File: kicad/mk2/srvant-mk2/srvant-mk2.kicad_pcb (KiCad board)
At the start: 2 copper layers, 5.9 x 5.8 mm, 245 parts, among them J1 Barrel_Jack_Switch, J10 HDMI connector, J2 Conn_01x02, J3 Conn_01x03, J4 USB_OTG, J5 ARJM11, J6 Conn_02x05_Odd_Even, J7 USB[690-008-221-904], J8 Bus_M.2_Socket_M, J9 ARJM11, Q1 DMP3013SFV-7, SW1 SW_DIP_x04, U1 AP63205WU, U10 TPD4EUSB30, U11 TPD4EUSB30, U12 KSZ9131RNXI-TR, U13 RT9742SNGV, U14 AP22653W6, U15 TLV62585DRLR, U16 FSUSB42MUX, U17 USB2514B-I/M2, U18 74LVC1G07SE-7, U19 TPD4EUSB30, U2 AP64501SP-13, U20 TPD4EUSB30, U3 74AHC1G32, U4 INA219AxDCN, U5 rp-t113-s3, U6 PCF85063AT/AAZ, U7 TPD4EUSB30, U8 74LVC2G07, U9 AP22653W6, Y1 X32K768S301, Y2 25Mhz, Y3 24MHz

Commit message: save state
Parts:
- removed C42, C92, C93: 100n, Capacitor_SMD:C_0402_1005Metric
- removed C83, C84, C85, C86, C87, C91: 10u, Capacitor_SMD:C_0805_2012Metric
- removed FB4, FB6, FB7: 220R, Resistor_SMD:R_0402_1005Metric
- removed J6: Conn_02x05_Odd_Even, Connector_PinHeader_2.54mm:PinHeader_2x05_P2.54mm_Vertical
- removed J7: USB[690-008-221-904], footprints:MOLEX_USB_67298-4090
- removed R26, R31, R35, R43, R45, R52: 10K, Resistor_SMD:R_0402_1005Metric
- removed R27, R32, R49: 1K, Resistor_SMD:R_0402_1005Metric
- removed R56: 22K 1%, Resistor_SMD:R_0402_1005Metric
- removed R61: 36K/1%, Resistor_SMD:R_0402_1005Metric
- removed TP13: TestPoint, TestPoint:TestPoint_Pad_2.0x2.0mm
- removed TP7, TP8, TP9: TestPoint, TestPoint:TestPoint_Pad_D1.0mm
- added D9: PESD2USB5UX-T, Package_TO_SOT_SMD:SOT-23, F.Cu at (84.8, 54.9)
- added FB9: 220R, Resistor_SMD:R_0402_1005Metric, F.Cu at (35.4, 177.3)
- added J11: USB A, footprints:CONN_GSB19110KEU_AMP, F.Cu at (39.4, 186.6)
- added R57: 510K 1%, Resistor_SMD:R_0402_1005Metric, F.Cu at (30.2, 60.2)
- added R69: 0, Resistor_SMD:R_0402_1005Metric, F.Cu at (44.1, 123.5)
- added R70: 0, Resistor_SMD:R_0402_1005Metric, F.Cu at (43.0, 123.5)
- added R71: 3.3K, Resistor_SMD:R_0402_1005Metric, F.Cu at (27.1, 136.6)
- added R72: 3.3K, Resistor_SMD:R_0402_1005Metric, F.Cu at (27.1, 138.1)
- added R73: 0, Resistor_SMD:R_0402_1005Metric, F.Cu at (81.9, 56.9)
- added SW2: EMMC_KEY, button-1571563-4:SW4_FSM-5P23_TEC, F.Cu at (82.4, 45.8)
- added SW3: RST, button-1571563-4:SW4_FSM-5P23_TEC, F.Cu at (89.9, 45.9)
- added SW4: HOST_RESET, footprints:button-SW_TL3340AF160QG, F.Cu at (46.9, 196.3)
- added TP16: +5v BMC, TestPoint:TestPoint_Pad_D1.0mm, B.Cu at (25.6, 78.4)
- added TP17: 5v OTG, TestPoint:TestPoint_Pad_D1.0mm, B.Cu at (52.9, 40.4)
- added TP18: ~, TestPoint:TestPoint_Pad_1.0x1.0mm, B.Cu at (45.8, 167.5)
- added TP19: NMI_N, TestPoint:TestPoint_Pad_D1.0mm, B.Cu at (33.2, 42.5)
- added U21: 74LVC1G07SE-7, Package_TO_SOT_SMD:SOT-353_SC-70-5, F.Cu at (27.1, 58.1)
- added U22: TMP1075DSG, Package_SON:WSON-8-1EP_2x2mm_P0.5mm_EP0.9x1.6mm_ThermalVias, F.Cu at (33.8, 123.6)
- added U23: SLB9670VQ20FW785XTMA1, QFN32_SLB9670VQ20FW785XTMA1_INF:QFN32_SLB9670VQ20FW785XTMA1_INF, F.Cu at (20.0, 109.5)
- added U24: 74AHC1G08, Package_TO_SOT_SMD:SOT-23-5_HandSoldering, F.Cu at (34.0, 58.2)
- added U25: 74AHC1G08, Package_TO_SOT_SMD:SOT-23-5, F.Cu at (79.2, 56.4)
- C33: value 10u -> 10u/35v; footprint Capacitor_SMD:C_0805_2012Metric -> Capacitor_SMD:C_0402_1005Metric
- C34: value 100u -> 100n; footprint Capacitor_Tantalum_SMD:CP_EIA-7343-31_Kemet-D -> Capacitor_SMD:C_0402_1005Metric
- C35, C36, C38, C39, C82, C90: value 10u -> 100n; footprint Capacitor_SMD:C_0805_2012Metric -> Capacitor_SMD:C_0402_1005Metric
- C40, C58, C59, C60, C61, C62: value 10u/35v -> 100n
- C49, C52, C53, C54, C56: value 100n -> 10u/35v
- C67, C68: value 100n -> 15p
- C69, C71: value 100n -> 10u 35v; footprint Capacitor_SMD:C_0402_1005Metric -> Capacitor_SMD:C_0805_2012Metric
- C70, C78, C79: value 100n -> 10u; footprint Capacitor_SMD:C_0402_1005Metric -> Capacitor_SMD:C_0805_2012Metric
- C73: value 15p -> 100n
- C74: value 15p -> 100u; footprint Capacitor_SMD:C_0402_1005Metric -> Capacitor_Tantalum_SMD:CP_EIA-7343-31_Kemet-D
- C75, C77: value 10u 35v -> 10u
- C80: value 100u -> 10u; footprint Capacitor_Tantalum_SMD:CP_EIA-7343-31_Kemet-D -> Capacitor_SMD:C_0805_2012Metric
- C88, C89: value 27p -> 100n
- C94: value 100n -> 1u; footprint Capacitor_SMD:C_0402_1005Metric -> Capacitor_SMD:C_0805_2012Metric
- R15: value 15K/1% -> 330R
- R18: value 330R -> 22R
- R24, R42: value 22R -> 10K
- R28, R33, R47, R50: value 10K -> 1K
- R29: value 1K -> 6.04K
- R30: value 6.04K -> 10K
- R34, R44, R46, R51: value 1K -> 10K
- R36: value 1K -> 22R
- R53: value 1K -> 15K/1%
- R54: value 15K/1% -> 100K 1%
- R55: value 100K 1% -> 22K 1%
- R59: value 36K/1% -> 510K 1%
- R62, R64: value 36K/1% -> 0
- R63: value 12K/1% -> 0
- SW1: value SW_DIP_x04 -> POWER; footprint DIP_SWITCH_DS04-254-2-04BK-SMT:DS04-254-2-04BK-SMT_CUD -> footprints:button-SW_TL3340AF160QG
- TP1: value TestPoint (VIN) -> VIN; moved to B.Cu
- TP10: value TestPoint -> PHY_AVDDH(3.3v); moved to B.Cu
- TP11: footprint TestPoint:TestPoint_Pad_2.0x2.0mm -> TestPoint:TestPoint_Pad_D1.0mm; moved to B.Cu
- TP12: value TestPoint -> 3v3_PCIe; footprint TestPoint:TestPoint_Pad_1.5x1.5mm -> TestPoint:TestPoint_Pad_D1.0mm; moved to B.Cu
- TP14: value TestPoint -> PCIe_nCLKREQ; footprint TestPoint:TestPoint_Pad_2.0x2.0mm -> TestPoint:TestPoint_Pad_D1.0mm; moved to B.Cu
- TP15: value TestPoint -> PCIe_nRST; footprint TestPoint:TestPoint_Pad_2.0x2.0mm -> TestPoint:TestPoint_Pad_D1.0mm; moved to B.Cu
- TP2: value TestPoint -> +5v HOST; moved to B.Cu
- TP3: value TestPoint -> GND; footprint TestPoint:TestPoint_Pad_2.0x2.0mm -> TestPoint:TestPoint_Pad_D1.0mm; moved to B.Cu
- TP4: value TestPoint -> 1v2; footprint TestPoint:TestPoint_Pad_2.0x2.0mm -> TestPoint:TestPoint_Pad_D1.0mm; moved to B.Cu
- TP5: value TestPoint -> 3.3v BMC; footprint TestPoint:TestPoint_Pad_2.0x2.0mm -> TestPoint:TestPoint_Pad_D1.0mm; moved to B.Cu
- TP6: value TestPoint -> VIN; moved to B.Cu
- U13: value RT9742SNGV -> 74AHC1G04; footprint Package_TO_SOT_SMD:SOT-23 -> Package_TO_SOT_SMD:SOT-23-5
- U17: value USB2514B-I/M2 -> PCF85063AT/AAZ; footprint Package_DFN_QFN:QFN-36-1EP_6x6mm_P0.5mm_EP3.7x3.7mm -> Package_SO:SOIC-8_3.9x4.9mm_P1.27mm
- U9: value AP22653W6 -> RT9742SNGV; footprint Package_TO_SOT_SMD:SOT-23-6 -> Package_TO_SOT_SMD:SOT-23
- Y3: value 24MHz -> X32K768S301; footprint footprints:LFXTAL-25MHz -> Crystal:Crystal_SMD_3215-2Pin_3.2x1.5mm
- moved C37 203.1 mm to (14.7, 147.5)
- moved R9 201.1 mm to (27.1, 145.8)
- moved R10 200.5 mm to (27.1, 146.9)
- moved D6 196.9 mm to (69.3, 183.5), turned to 90 degrees
- moved TP4 192.6 mm to (68.5, 180.6), turned to 180 degrees
- moved R13 191.3 mm to (16.7, 149.1)
- moved R14 191.0 mm to (16.7, 150.7)
- moved U13 189.8 mm to (41.8, 169.3), turned to 180 degrees
- moved C33 184.5 mm to (60.4, 164.6), turned to 180 degrees
- moved R6 184.3 mm to (13.1, 77.9), turned to 90 degrees
- moved U8 184.1 mm to (14.1, 144.9), turned to -90 degrees
- moved C34 183.8 mm to (60.4, 165.7), turned to 180 degrees
- moved D3 183.6 mm to (14.0, 149.1), turned to 180 degrees
- moved R11 182.1 mm to (27.1, 143.0), turned to 180 degrees
- moved C36 180.1 mm to (62.7, 164.6), turned to 180 degrees
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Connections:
- net /bmc/EPHY_25M renamed /BMC ethernet/EPHY_25M
- net /bmc/RESET_OUT_N renamed /BMC ethernet/RESET_OUT_N
- net /bmc/TXRXA_N renamed /BMC ethernet/TXRXA_N
- net /bmc/TXRXA_P renamed /BMC ethernet/TXRXA_P
- net /bmc/TXRXB_N renamed /BMC ethernet/TXRXB_N
- net /bmc/TXRXB_P renamed /BMC ethernet/TXRXB_P
- net /bmc/TXRXC_N renamed /BMC ethernet/TXRXC_N
- net /bmc/TXRXC_P renamed /BMC ethernet/TXRXC_P
- net /bmc/TXRXD_N renamed /BMC ethernet/TXRXD_N
- net /bmc/TXRXD_P renamed /BMC ethernet/TXRXD_P
- net /cm4/GPIO12 renamed /cm4/HOST_SDA5
- net /cm4/GPIO13 renamed /cm4/HOST_SCL5
- net /cm4/GPIO4 renamed /cm4/HOST_SPI4_CE0
- net /cm4/GPIO5 renamed /cm4/HOST_SPI4_MISO
- net /cm4/GPIO6 renamed /cm4/HOST_SPI4_MOSI
- net /cm4/GPIO7 renamed /cm4/HOST_SPI4_SCLK
- C100 pad 1: /cm4/+3V3 PCIe -> /cm4/+3.3v_HOST_PCIe
- C101 pad 1: /cm4/+3V3 PCIe -> /cm4/+3.3v_HOST_PCIe
- C102 pad 1: /cm4/+3V3 PCIe -> /cm4/+3.3v_HOST_PCIe
- C103 pad 1: /cm4/+3V3 PCIe -> /cm4/+3.3v_HOST_PCIe
- C20 pad 1: /power/+5v_HOST -> /cm4/+5v_HOST
- C23 pad 1: /power/+5v_HOST -> /cm4/+5v_HOST
- C25 pad 1: /power/+5v_HOST -> /cm4/+5v_HOST
- C26 pad 1: /power/+5v_HOST -> /cm4/+5v_HOST
- C27 pad 1: /power/+5v_HOST -> /cm4/+5v_HOST
- C28 pad 1: /power/+5v_HOST -> /cm4/+5v_HOST
- C30 pad 1: /bmc/3.3v_BMC -> /BMC ethernet/3.3v_BMC
- C31 pad 1: /bmc/3.3v_BMC -> /BMC ethernet/3.3v_BMC
- C33 pad 1: /bmc/+5v_BMC -> /BMC ethernet/1V2
- C34 pad 1: /bmc/+5V_OTG -> /BMC ethernet/1V2
- C35 pad 1: /bmc/+5V_OTG -> /BMC ethernet/1V2
- C36 pad 1: /bmc/+5V_OTG -> /BMC ethernet/1V2
- C37 pad 1: /bmc/3.3v_BMC -> /BMC ethernet/3.3v_BMC
- C38 pad 1: /bmc/+5V_OTG -> /BMC ethernet/1V2
- C39 pad 1: /bmc/+5V_OTG -> /BMC ethernet/1V2
- C40 pad 1: /bmc/PHY_DVDDL -> Net-(C40-Pad1)
- C41 pad 1: /bmc/PHY_DVDDL -> /BMC ethernet/1V2
- C43 pad 1: /bmc/PHY_DVDDL -> /BMC ethernet/1V2
- C44 pad 1: /bmc/PHY_AVDDL_PLL -> Net-(C44-Pad1)
- C45 pad 1: /bmc/PHY_DVDDL -> /BMC ethernet/1V2
- C46 pad 1: Net-(C46-Pad1) -> /BMC ethernet/1V2
- C47 pad 1: /bmc/PHY_AVDDL -> /BMC ethernet/1V2
- C48 pad 1: /bmc/PHY_AVDDL_PLL -> /BMC ethernet/1V2
- C49 pad 1: /bmc/PHY_DVDDL -> /BMC ethernet/1V2
- C50 pad 1: Net-(C50-Pad1) -> /BMC ethernet/1V2
- C51 pad 1: /bmc/PHY_AVDDL -> /BMC ethernet/1V2
- C52 pad 1: /bmc/PHY_AVDDL_PLL -> /BMC ethernet/1V2
- C53 pad 1: /bmc/PHY_DVDDL -> /BMC ethernet/PHY_RESET_N
- C54 pad 1: /bmc/PHY_AVDDL -> /BMC ethernet/3.3v_PHY
- C55 pad 1: /bmc/PHY_AVDDL_PLL -> Net-(U12-LDO_O)
- C56 pad 1: /bmc/PHY_DVDDL -> /BMC ethernet/3.3v_PHY
- C57 pad 1: /bmc/PHY_AVDDL -> /BMC ethernet/3.3v_PHY
- C58 pad 1: /bmc/PHY_AVDDL -> Net-(U12-LDO_O)
- C59 pad 1: /bmc/PHY_RESET_N -> /BMC ethernet/3.3v_PHY
- C60 pad 1: /bmc/PHY_AVDDH -> /BMC ethernet/3.3v_PHY
- C61 pad 1: /bmc/1V2 -> /BMC ethernet/3.3v_PHY
- C62 pad 1: /bmc/PHY_DVDDH -> /BMC ethernet/3.3v_PHY
- C63 pad 1: /bmc/PHY_AVDDH -> /BMC ethernet/3.3v_PHY
- C64 pad 1: /bmc/1V2 -> /BMC ethernet/3.3v_PHY
- C65 pad 1: /bmc/PHY_DVDDH -> /BMC ethernet/3.3v_PHY
- C66 pad 1: /bmc/PHY_AVDDH -> /BMC ethernet/3.3v_PHY
- C67 pad 1: /bmc/PHY_DVDDH -> GND
- C67 pad 2: GND -> Net-(U12-XI)
- C68 pad 1: /bmc/PHY_AVDDH -> Net-(U12-XO)
- C69 pad 1: /bmc/PHY_DVDDH -> /cm4/+5v_HOST
- C70 pad 1: /bmc/PHY_AVDDH -> /cm4/+5v_HOST
- C71 pad 1: /bmc/PHY_DVDDH -> /cm4/+5v_HOST
- C72 pad 1: /bmc/PHY_DVDDH -> /cm4/+5v_HOST
- C73 pad 1: GND -> /cm4/+5v_HOST_HDMI
- C73 pad 2: Net-(U12-XI) -> GND
- C74 pad 1: Net-(U12-XO) -> /cm4/+5v_HOST_VBUS
- C75 pad 1: /cm4/+5v_HOST -> /cm4/+5v_HOST_VBUS
- C76 pad 1: /cm4/+5v_HOST -> /cm4/+3.3v_HOST_PCIe
- C77 pad 1: /cm4/+5v_HOST -> /cm4/+5v_HOST_VBUS
- C78 pad 1: /cm4/+5v_HOST -> /cm4/+3.3v_HOST_PCIe
- C79 pad 1: /cm4/HDMI_5v -> /cm4/+5v_HOST_VBUS
- C80 pad 1: /cm4/VBUS -> /cm4/+3.3v_HOST_PCIe
- C81 pad 1: /cm4/VBUS -> /cm4/+5v_HOST_VBUS
- C82 pad 1: /cm4/VBUS -> /BMC ethernet/3.3v_BMC
- C88 pad 1: /cm4/XTALIN -> /cm4/+BATT
- C89 pad 1: /cm4/XTALOUT -> /cm4/+5v_HOST
- C90 pad 1: /cm4/+3.3v_HOST -> Net-(C90-Pad1)
- C90 pad 2: GND -> Net-(C90-Pad2)
- C95 pad 1: /cm4/+3.3v_HOST -> GND
- C95 pad 2: GND -> /cm4/+3.3v_HOST
- C96 pad 1: /cm4/+3.3v_HOST -> GND
- C96 pad 2: GND -> /cm4/+3.3v_HOST
- C97 pad 1: /cm4/+3.3v_HOST -> GND
- C97 pad 2: GND -> /cm4/+3.3v_HOST
- C98 pad 1: /cm4/+3V3 PCIe -> /cm4/+3.3v_HOST_PCIe
- C99 pad 1: /cm4/+3V3 PCIe -> /cm4/+3.3v_HOST_PCIe
- D2 pad 2: /bmc/3.3v_BMC -> /BMC ethernet/3.3v_BMC
- D3 pad 2: /bmc/3.3v_BMC -> /BMC ethernet/3.3v_BMC
- D4 pad 2: /bmc/+3.3v -> /BMC ethernet/3.3v_BMC
- D5 pad 1: /bmc/PHY_DVDDH -> /BMC ethernet/3.3v_PHY
- D5 pad 2: /bmc/PHY_RESET_N -> /BMC ethernet/PHY_RESET_N
- D6 pad 2: /bmc/PHY_RESET_N -> /BMC ethernet/PHY_RESET_N
- FB2 pad 1: /bmc/1V2 -> /BMC ethernet/3.3v_PHY
- FB2 pad 2: /bmc/PHY_DVDDL -> /BMC ethernet/3.3v_BMC
- FB3 pad 1: /bmc/1V2 -> Net-(U12-LDO_O)
- FB3 pad 2: /bmc/PHY_AVDDL_PLL -> /BMC ethernet/1V2
- J10 pad 18: /cm4/HDMI_5v -> /cm4/+5v_HOST_HDMI
- J2 pad 2: /bmc/3.3v_BMC -> /BMC ethernet/3.3v_BMC
- J4 pad 1: /bmc/+5V_OTG -> /bmc/+5V_BMC_OTG
- J5 pad 11: /bmc/PHY_DVDDH -> /BMC ethernet/3.3v_PHY
- J5 pad 13: /bmc/PHY_DVDDH -> /BMC ethernet/3.3v_PHY
- J5 pad 5: Net-(C46-Pad1) -> Net-(C40-Pad1)
- J5 pad 6: Net-(C50-Pad1) -> Net-(C44-Pad1)
- J8 pad 12: /cm4/+3V3 PCIe -> /cm4/+3.3v_HOST_PCIe
- J8 pad 14: /cm4/+3V3 PCIe -> /cm4/+3.3v_HOST_PCIe
- J8 pad 16: /cm4/+3V3 PCIe -> /cm4/+3.3v_HOST_PCIe
- J8 pad 18: /cm4/+3V3 PCIe -> /cm4/+3.3v_HOST_PCIe
- J8 pad 2: /cm4/+3V3 PCIe -> /cm4/+3.3v_HOST_PCIe
- J8 pad 4: /cm4/+3V3 PCIe -> /cm4/+3.3v_HOST_PCIe
- J8 pad 70: /cm4/+3V3 PCIe -> /cm4/+3.3v_HOST_PCIe
- J8 pad 72: /cm4/+3V3 PCIe -> /cm4/+3.3v_HOST_PCIe
- J8 pad 74: /cm4/+3V3 PCIe -> /cm4/+3.3v_HOST_PCIe
- L2 pad 2: /power/+5v_HOST -> /cm4/+5v_HOST
- L3 pad 2: /cm4/+3V3 PCIe -> /cm4/+3.3v_HOST_PCIe
- Module1 pad 20: /cm4/EEPROM_nWP -> /bmc/BMC_HOST_EEPROM_nWP
- Module1 pad 25: /cm4/GPIO21 -> /cm4/HOST_SPI1_SCLK
- Module1 pad 26: /cm4/GPIO19 -> /cm4/HOST_SPI1_MISO
- Module1 pad 27: /cm4/GPIO20 -> /cm4/HOST_SPI1_MOSI
- Module1 pad 39: /cm4/GPIO8 -> /bmc/BMC_UART1_RX
- Module1 pad 40: /cm4/GPIO9 -> /bmc/BMC_UART1_TX
- Module1 pad 49: /cm4/GPIO18 -> /cm4/HOST_SPI1_CE0_N
- Module1 pad 51: /cm4/HOST_UART_TX -> /bmc/BMC_UART0_TX
- Module1 pad 55: /cm4/HOST_UART_RX -> /bmc/BMC_UART0_RX
- Module1 pad 80: /cm4/SCL0 -> /cm4/HOST_SCL0
- Module1 pad 82: /cm4/SDA0 -> /cm4/HOST_SDA0
- Module1 pad 89: /cm4/WL_nDis -> /bmc/BMC_HOST_BT_nDis
- Module1 pad 91: /cm4/BT_nDis -> /bmc/BMC_HOST_WL_nDis
- Module1 pad 92: /cm4/HOST_RUN_PG -> /bmc/BMC_HOST_POST_COMPLETE
- Module1 pad 93: /cm4/HOST_nRPIBOOT -> /bmc/BMC_HOST_nRPIBOOT
- R10 pad 1: /bmc/3.3v_BMC -> /BMC ethernet/3.3v_BMC
- R11 pad 2: /bmc/3.3v_BMC -> /BMC ethernet/3.3v_BMC
- R12 pad 2: /bmc/3.3v_BMC -> /BMC ethernet/3.3v_BMC
- R15 pad 1: Net-(U9-ILIM) -> Net-(J5-LED2-)
- R15 pad 2: GND -> /BMC ethernet/PHY_LED_LINK / PHYAD1
- R16 pad 1: /bmc/3.3v_BMC -> /BMC ethernet/3.3v_BMC
- R17 pad 1: Net-(J5-LED2-) -> Net-(J5-LED1-)
- R17 pad 2: /bmc/PHY_LED_LINK / PHYAD1 -> /BMC ethernet/PHY_LED_ACT / PHYAD0
- R18 pad 1: Net-(J5-LED1-) -> Net-(U12-TXD0)
- R18 pad 2: /bmc/PHY_LED_ACT / PHYAD0 -> /BMC ethernet/TXD0
- R19 pad 1: Net-(U12-TXD0) -> Net-(U12-TXD1)
- R19 pad 2: /bmc/TXD0 -> /BMC ethernet/TXD1
- R20 pad 1: Net-(U12-TXD1) -> Net-(U12-TXD2)
- R20 pad 2: /bmc/TXD1 -> /BMC ethernet/TXD2
- R21 pad 1: Net-(U12-TXD2) -> Net-(U12-TXD3)
- R21 pad 2: /bmc/TXD2 -> /BMC ethernet/TXD3
- R22 pad 1: Net-(U12-TXD3) -> Net-(U12-TXC)
- R22 pad 2: /bmc/TXD3 -> /BMC ethernet/TXC
- R23 pad 1: Net-(U12-TXC) -> Net-(U12-TX_CTL)
- R23 pad 2: /bmc/TXC -> /BMC ethernet/TX_CTL
- R24 pad 1: Net-(U12-TX_CTL) -> /BMC ethernet/PHY_RESET_N
- R24 pad 2: /bmc/TX_CTL -> /BMC ethernet/3.3v_PHY
- R25 pad 1: /bmc/PHY_RESET_N -> /BMC ethernet/3.3v_PHY
- R25 pad 2: /bmc/PHY_DVDDH -> /BMC ethernet/CLK125_OUT / LED_MODE
- R28 pad 1: /bmc/PHY_DVDDH -> /BMC ethernet/CLK125_EN
- R28 pad 2: /bmc/CLK125_EN -> GND
- R29 pad 1: /bmc/CLK125_EN -> GND
- R29 pad 2: GND -> Net-(U12-ISET)
- R30 pad 1: GND -> /BMC ethernet/3.3v_PHY
- R30 pad 2: Net-(U12-ISET) -> /BMC ethernet/MODE0
- R33 pad 1: /bmc/PHY_DVDDH -> /BMC ethernet/PHYAD2
- R33 pad 2: /bmc/PHYAD2 -> GND
- R34 pad 1: /bmc/PHYAD2 -> /BMC ethernet/3.3v_PHY
- R34 pad 2: GND -> /BMC ethernet/MODE1
- R36 pad 1: /bmc/MODE1 -> /BMC ethernet/RXC
- R36 pad 2: GND -> /BMC ethernet/PHYAD2
- R37 pad 1: /bmc/RXC -> /BMC ethernet/RX_CTL
- R37 pad 2: /bmc/PHYAD2 -> /BMC ethernet/CLK125_EN
- R38 pad 1: /bmc/RX_CTL -> /BMC ethernet/RXD0
- R38 pad 2: /bmc/CLK125_EN -> /BMC ethernet/MODE0
- R39 pad 1: /bmc/RXD0 -> /BMC ethernet/RXD1
- R39 pad 2: /bmc/MODE0 -> /BMC ethernet/MODE1
- R40 pad 1: /bmc/RXD1 -> /BMC ethernet/RXD2
- R40 pad 2: /bmc/MODE1 -> /BMC ethernet/MODE2
- R41 pad 1: /bmc/RXD2 -> /BMC ethernet/RXD3
- R41 pad 2: /bmc/MODE2 -> /BMC ethernet/MODE3
- R42 pad 1: /bmc/RXD3 -> /BMC ethernet/3.3v_PHY
- R42 pad 2: /bmc/MODE3 -> /BMC ethernet/MODE2
- R44 pad 1: /bmc/MODE2 -> /BMC ethernet/3.3v_PHY
- R44 pad 2: GND -> /BMC ethernet/PHY_LED_LINK / PHYAD1
- R46 pad 1: /bmc/PHY_LED_LINK / PHYAD1 -> /BMC ethernet/3.3v_PHY
- R46 pad 2: GND -> /BMC ethernet/PHY_INT_N
- R47 pad 1: /bmc/PHY_DVDDH -> /BMC ethernet/3.3v_PHY
- R47 pad 2: /bmc/PHY_INT_N -> /BMC ethernet/PHY_MDIO
- R48 pad 1: /bmc/PHY_DVDDH -> /BMC ethernet/3.3v_PHY
- R48 pad 2: /bmc/PHY_MDIO -> /BMC ethernet/PHY_MDC
- R5 pad 1: /power/+5v_HOST -> /cm4/+5v_HOST
- R50 pad 1: /bmc/PHY_DVDDH -> /BMC ethernet/MODE3
- R50 pad 2: /bmc/MODE3 -> GND
- R51 pad 1: /bmc/MODE3 -> /BMC ethernet/3.3v_PHY
- R51 pad 2: GND -> /BMC ethernet/PHY_LED_ACT / PHYAD0
- R53 pad 1: /bmc/PHY_LED_ACT / PHYAD0 -> Net-(U14-ILIM)
- R54 pad 1: Net-(U14-ILIM) -> /cm4/+3.3v_HOST_PCIe
- R54 pad 2: GND -> /power/3V3P_FB
- R55 pad 1: /cm4/+3V3 PCIe -> /power/3V3P_FB
- R55 pad 2: /cm4/3V3P_FB -> GND
- R59 pad 1: Net-(U17-SCL/SMBCLK/CFG_SEL0) -> Net-(C90-Pad1)
- R59 pad 2: GND -> /cm4/+5v_HOST
- R62 pad 1: Net-(U17-SUSP_IND/LOCAL_PWR/NON_REM0) -> /bmc/BMC_HOST_POST_COMPLETE
- R62 pad 2: GND -> Net-(U5A-PE_EINT7)
- R63 pad 1: GND -> /bmc/BMC_HOST_nRPIBOOT
- R63 pad 2: Net-(U17-RBIAS) -> Net-(U5A-PE_EINT6)
- R64 pad 1: Net-(U17-HS_IND/CFG_SEL1) -> /bmc/BMC_HOST_EEPROM_nWP
- R64 pad 2: GND -> Net-(U5A-PE_EINT4)
- R9 pad 1: /bmc/3.3v_BMC -> /BMC ethernet/3.3v_BMC
- SW1 pad 1: unconnected-(SW1-Pad1) -> /bmc/BMC_HOST_POWER_BUTTON
- SW1 pad 3: GND -> (no net)
- TP10 pad 1: /bmc/PHY_AVDDH -> /BMC ethernet/3.3v_PHY
- TP12 pad 1: /cm4/+3V3 PCIe -> /cm4/+3.3v_HOST_PCIe
- TP14 pad 1: /cm4/PCIe_nCLKREQ -> /cm4/PCIE_nRST
- TP15 pad 1: /cm4/PCIe_nRST -> /cm4/PCIE_CLK_nREQ
- TP2 pad 1: /power/+5v_HOST -> /cm4/+5v_HOST
- TP4 pad 1: Net-(D3-K) -> /BMC ethernet/1V2
- TP5 pad 1: Net-(D4-K) -> /BMC ethernet/3.3v_BMC
- TP6 pad 1: /bmc/PHY_DVDDH -> /power/3V3P_FB
- U12 pad 1: /bmc/PHY_AVDDH -> /BMC ethernet/3.3v_PHY
- U12 pad 12: /bmc/PHY_AVDDH -> /BMC ethernet/3.3v_PHY
- U12 pad 15: /bmc/PHY_LED_LINK / PHYAD1 -> /BMC ethernet/PHY_LED_LINK / PHYAD1
- U12 pad 16: /bmc/PHY_DVDDH -> /BMC ethernet/3.3v_PHY
- U12 pad 17: /bmc/PHY_LED_ACT / PHYAD0 -> /BMC ethernet/PHY_LED_ACT / PHYAD0
- U12 pad 18: /bmc/PHY_DVDDL -> /BMC ethernet/1V2
- U12 pad 23: /bmc/PHY_DVDDL -> /BMC ethernet/1V2
- U12 pad 26: /bmc/PHY_DVDDL -> /BMC ethernet/1V2
- U12 pad 27: /bmc/MODE3 -> /BMC ethernet/MODE3
- U12 pad 28: /bmc/MODE2 -> /BMC ethernet/MODE2
- U12 pad 30: /bmc/PHY_DVDDL -> /BMC ethernet/1V2
- U12 pad 31: /bmc/MODE1 -> /BMC ethernet/MODE1
- U12 pad 32: /bmc/MODE0 -> /BMC ethernet/MODE0
- U12 pad 33: /bmc/CLK125_EN -> /BMC ethernet/CLK125_EN
- U12 pad 34: /bmc/PHY_DVDDH -> /BMC ethernet/3.3v_PHY
- U12 pad 35: /bmc/PHYAD2 -> /BMC ethernet/PHYAD2
- U12 pad 36: /bmc/PHY_MDC -> /BMC ethernet/PHY_MDC
- U12 pad 37: /bmc/PHY_MDIO -> /BMC ethernet/PHY_MDIO
- U12 pad 38: /bmc/PHY_INT_N -> /BMC ethernet/PHY_INT_N
- U12 pad 39: /bmc/PHY_DVDDL -> /BMC ethernet/1V2
- U12 pad 4: /bmc/PHY_AVDDL -> /BMC ethernet/1V2
- U12 pad 40: /bmc/PHY_DVDDH -> /BMC ethernet/3.3v_PHY
- U12 pad 41: /bmc/CLK125_OUT / LED_MODE -> /BMC ethernet/CLK125_OUT / LED_MODE
- U12 pad 42: /bmc/PHY_RESET_N -> /BMC ethernet/PHY_RESET_N
- U12 pad 43: /bmc/1V2 -> Net-(U12-LDO_O)
- U12 pad 44: /bmc/PHY_AVDDL_PLL -> /BMC ethernet/1V2
- U12 pad 9: /bmc/PHY_AVDDL -> /BMC ethernet/1V2
- U13 pad 1: /cm4/+5v_HOST -> (no net)
- U13 pad 2: /cm4/HDMI_5v -> /cm4/USBOTG_ID
- U14 pad 3: /cm4/PWR1 -> Net-(U14-EN)
- U14 pad 6: /cm4/VBUS -> /cm4/+5v_HOST_VBUS
- U15 pad 5: /cm4/3V3P_FB -> /power/3V3P_FB
- U16 pad 6: /cm4/USBH_N -> /cm4/USB_OUT_N
- U16 pad 7: /cm4/USBH_P -> /cm4/USB_OUT_P
- U16 pad 8: /cm4/HOST_USB_N -> /bmc/BMC_USB_HOST_N
- U16 pad 9: /cm4/HOST_USB_P -> /bmc/BMC_USB_HOST_P
- U17 pad 1: /cm4/HD1_N -> Net-(U17-OSCI)
- U17 pad 2: /cm4/HD1_P -> Net-(U17-OSCO)
- U17 pad 3: /cm4/HD2_N -> /cm4/nRTC_INT
- U17 pad 4: /cm4/HD2_P -> GND
- U17 pad 5: /cm4/+3.3v_HOST -> /cm4/HOST_SDA0
- U17 pad 6: /cm4/HD3_N -> /cm4/HOST_SCL0
- U17 pad 7: /cm4/HD3_P -> unconnected-(U17-CLKO-Pad7)
- U17 pad 8: /cm4/HD4_N -> /cm4/+BATT
- U3 pad 5: /bmc/3.3v_BMC -> /BMC ethernet/3.3v_BMC
- U4 pad 4: /bmc/3.3v_BMC -> /BMC ethernet/3.3v_BMC
- U5 pad 118: /bmc/PHY_MDIO -> /BMC ethernet/PHY_MDIO
- U5 pad 119: /bmc/PHY_MDC -> /BMC ethernet/PHY_MDC
- U5 pad 121: /bmc/RX_CTL -> /BMC ethernet/RX_CTL
- U5 pad 122: /bmc/RXD0 -> /BMC ethernet/RXD0
- U5 pad 123: /bmc/RXD1 -> /BMC ethernet/RXD1
- U5 pad 124: /bmc/RXC -> /BMC ethernet/RXC
- U5 pad 125: /bmc/TXC -> /BMC ethernet/TXC
- U5 pad 126: /bmc/TXD0 -> /BMC ethernet/TXD0
- U5 pad 127: /bmc/TXD1 -> /BMC ethernet/TXD1
- U5 pad 128: /bmc/TX_CTL -> /BMC ethernet/TX_CTL
- U5 pad 130: /bmc/RXD3 -> /BMC ethernet/RXD3
- U5 pad 131: /bmc/RXD2 -> /BMC ethernet/RXD2
- U5 pad 132: /bmc/TXD3 -> /BMC ethernet/TXD3
- U5 pad 133: /bmc/TXD2 -> /BMC ethernet/TXD2
- U5 pad 30: /bmc/3.3v_BMC -> /BMC ethernet/3.3v_BMC
- U5 pad 35: unconnected-(U5B-EMMC_KEY-Pad35) -> /bmc/EMMC_KEY
- U5 pad 36: unconnected-(U5B-POWER_EN-Pad36) -> /bmc/+5v_BMC
- U5 pad 37: unconnected-(U5B-KEY_RST-Pad37) -> /bmc/RST_KEY
- U5 pad 42: /bmc/HOST_POST_COMPLETE -> /bmc/BMC_HOST_POWER_BUTTON
- U5 pad 43: /bmc/HOST_POWER_OUT -> /bmc/BMC_HOST_RESET_BUTTON
- U5 pad 44: unconnected-(U5A-UART1_RX-Pad44) -> /bmc/BMC_UART1_RX
- U5 pad 45: unconnected-(U5A-UART1_TX-Pad45) -> /bmc/BMC_UART1_TX
- U5 pad 48: /bmc/HOST_RESET_OUT -> Net-(U5A-PE_EINT7)
- U5 pad 49: /bmc/HOST_nRPIBOOT -> Net-(U5A-PE_EINT6)
- U5 pad 50: /bmc/HOST_EEPROM_nWP -> /cm4/USBOTG_ID
- U5 pad 51: /bmc/BMC_HOST_USB_DEMUX_CONTROL -> Net-(U5A-PE_EINT4)
- U5 pad 54: /power/BMC_HOST_POWER_EN -> Net-(U5A-PE_EINT1)
- U5 pad 55: unconnected-(U5A-PE_EINT0-Pad55) -> Net-(U5A-PE_EINT0)
- U5 pad 57: /bmc/BMC_ID_LED -> unconnected-(U5A-PD_EINT0-Pad57)
- U5 pad 61: /bmc/PHY_INT_N -> /BMC ethernet/PHY_INT_N
- U5 pad 66: /bmc/BMC_POWER_LED -> unconnected-(U5A-PD_EINT9-Pad66)
- U5 pad 72: unconnected-(U5A-PD_EINT15-Pad72) -> /bmc/BMC_HOST_BT_nDis
- U5 pad 73: unconnected-(U5A-PWM0-Pad73) -> /bmc/BMC_POWER_LED
- U5 pad 74: unconnected-(U5A-PWM1-Pad74) -> /bmc/BMC_ID_LED
- U5 pad 75: unconnected-(U5A-PWM2-Pad75) -> /bmc/BMC_HOST_POST_COMPLETE
- U5 pad 76: unconnected-(U5A-PWM3-Pad76) -> /bmc/BMC_HOST_POWER_OUT
- U5 pad 79: unconnected-(U5A-PWM7-Pad79) -> /bmc/BMC_TEMP_ALERT
- U5 pad 83: /bmc/BMC_I2C_1_SDA -> /cm4/GPIO10
- U5 pad 84: /bmc/BMC_I2C_1_SCK -> /cm4/GPIO11
- U6 pad 3: /bmc/NMI_N (XXX) -> /bmc/NMI_N
- U8 pad 5: /bmc/3.3v_BMC -> /BMC ethernet/3.3v_BMC
- U9 pad 1: /bmc/+5v_BMC -> /cm4/+5v_HOST
- U9 pad 2: GND -> /cm4/+5v_HOST_HDMI
- U9 pad 3: /bmc/USB0_DRV -> GND
- Y3 pad 1: /cm4/XTALIN -> Net-(U17-OSCO)
- Y3 pad 2: GND -> Net-(U17-OSCI)
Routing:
- net /BMC ethernet/3.3v_BMC: track 0.00 -> 552.1 mm, vias 0 -> 12
- net /cm4/+5v_HOST: track 0.00 -> 419.8 mm, vias 0 -> 27
- net GND: track 0.00 -> 290.3 mm, vias 0 -> 280
- net /cm4/+3.3v_HOST: track 0.00 -> 240.4 mm, vias 0 -> 9
- net /bmc/+5v_BMC: track 0.00 -> 214.7 mm, vias 0 -> 20
- net /bmc/BMC_HOST_RESET_BUTTON: track 0.00 -> 145.7 mm, vias 0 -> 2
- net /BMC ethernet/3.3v_PHY: track 0.00 -> 141.0 mm, vias 0 -> 12
- net /bmc/BMC_USB_OTG_P: track 0.00 -> 135.3 mm, vias 0 -> 2
- net /bmc/BMC_USB_OTG_N: track 0.00 -> 133.7 mm, vias 0 -> 2
- net /cm4/USBOTG_ID: track 0.00 -> 131.9 mm, vias 0 -> 5
- net /bmc/BMC_I2C_3_SCK: track 0.00 -> 130.6 mm, vias 0 -> 2
- net /bmc/BMC_I2C_3_SDA: track 0.00 -> 126.2 mm, vias 0 -> 2
- net /cm4/ETH_LEDY: track 0.00 -> 124.6 mm, vias 0 -> 3
- net /power/BMC_I2C_0_SDA: track 0.00 -> 123.8 mm, vias 0 -> 2
- net /cm4/ETH_LEDG: track 0.00 -> 122.2 mm, vias 0 -> 2
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- added copper zone on In1.Cu, net (none)
- added copper zone on In2.Cu, net (none)
- added copper zone on F.Cu, net /bmc/+5v_BMC
- added copper zone on F.Cu, net /cm4/+5v_HOST
- added copper zone on F.Cu, net /power/SENSE_IN+
- added copper zone on In2.Cu, net GND
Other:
- board size 5.9 x 5.8 mm -> 88 x 159 mm
- copper layers 2 -> 4
- board text added: "1u (44mm) x 2"

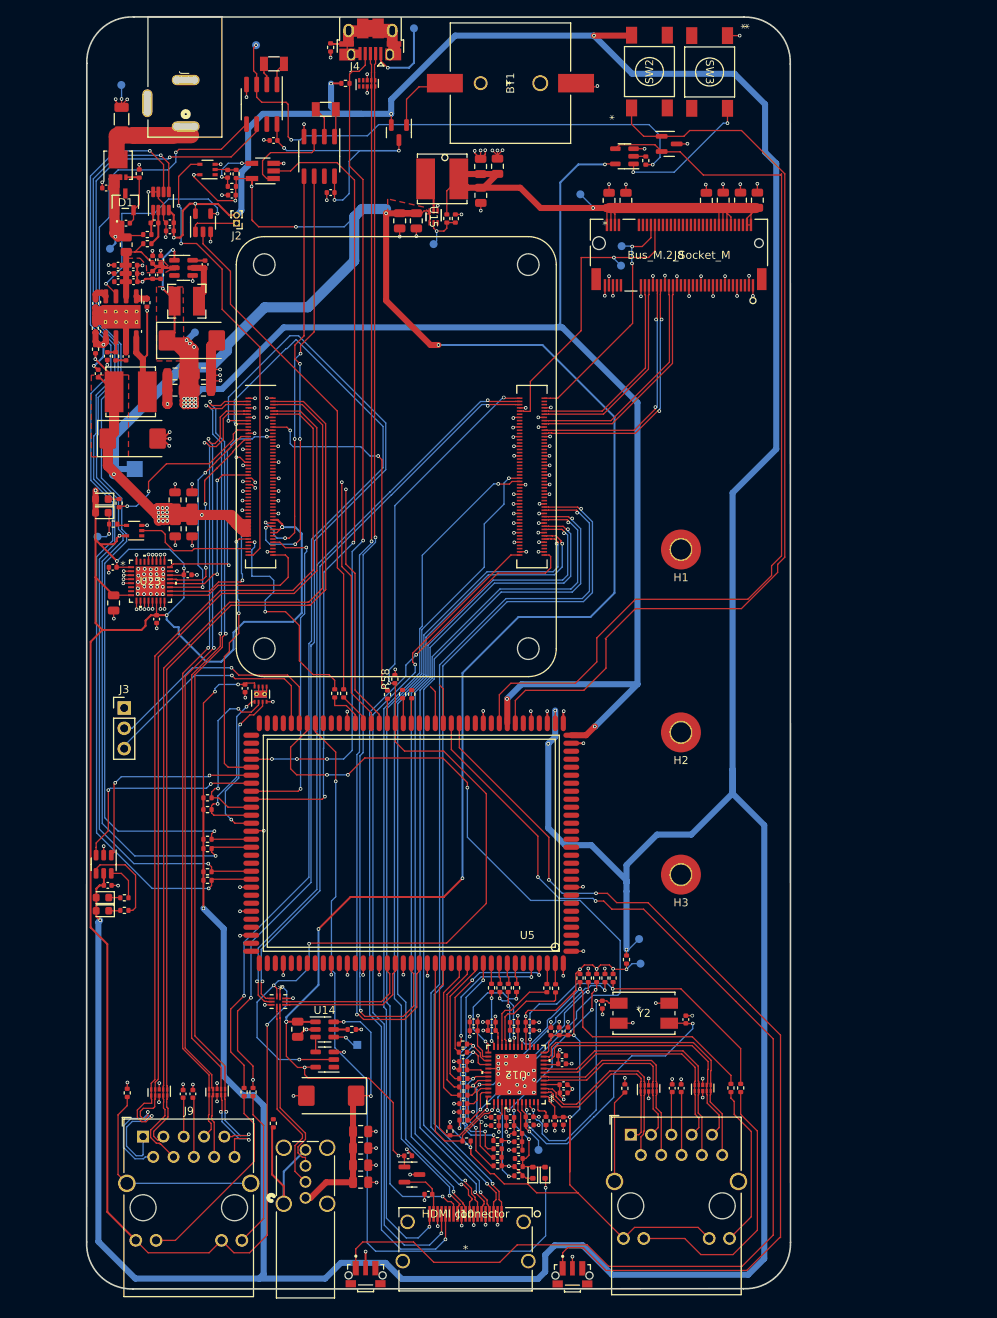
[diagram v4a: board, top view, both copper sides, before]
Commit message: mostly wired, impedance control, etc
Repositioned most of the components. Set impedance control based
on jlcpcb calculator.

Need to:
* reposition ethernet port to allow mounting hole.
* move power socket lower, reduce board size
* fix the rest of DRC errors.
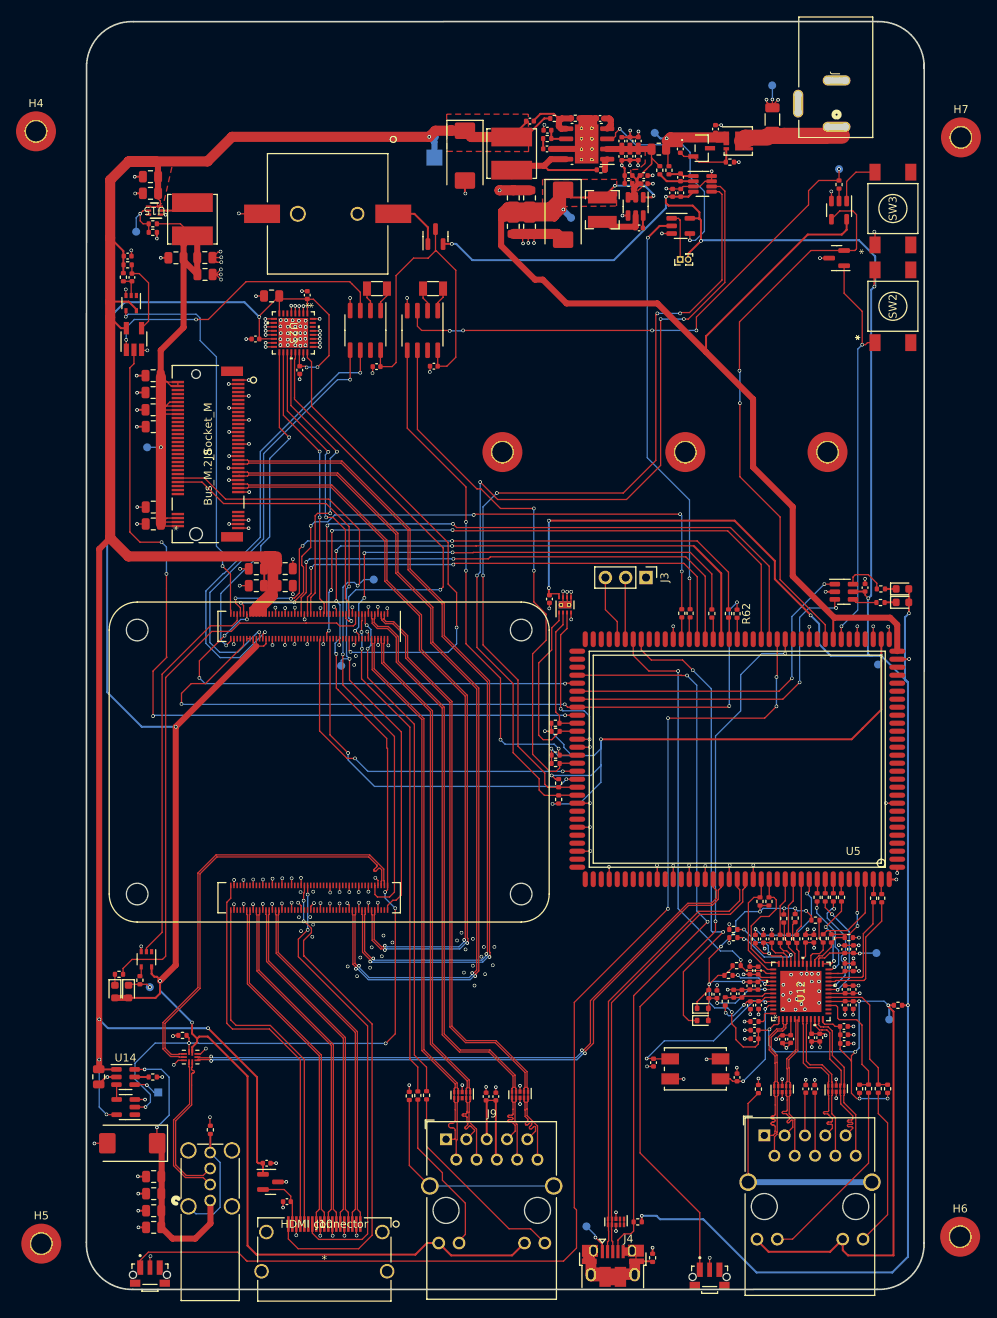
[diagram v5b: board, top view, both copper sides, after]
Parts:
- added H4: MountingHole, MountingHole:MountingHole_2.5mm_Pad_TopOnly, F.Cu at (5.69, 53.3)
- added H5: MountingHole, MountingHole:MountingHole_2.5mm_Pad_TopOnly, F.Cu at (6.35, 192.3)
- added H6: MountingHole, MountingHole:MountingHole_2.5mm_Pad_TopOnly, F.Cu at (121.2, 191.5)
- added H7: MountingHole, MountingHole:MountingHole_2.5mm_Pad_TopOnly, F.Cu at (121.3, 54.1)
- moved FB1 156.6 mm to (82.8, 194.1), turned to -90 degrees
- moved J4 156.3 mm to (77.8, 195.1), turned to 0 degrees
- moved TP17 151.3 mm to (74.5, 190.2)
- moved R16 146.9 mm to (80.9, 189.6), turned to 180 degrees
- moved U7 145.7 mm to (78.2, 189.6), turned to -90 degrees
- moved D3 107.2 mm to (114.0, 110.5), turned to 0 degrees
- moved D4 107.2 mm to (114.0, 112.2), turned to 0 degrees
- moved R13 102.1 mm to (111.3, 110.5), turned to 180 degrees
- moved R14 102.0 mm to (111.3, 112.2), turned to 180 degrees
- moved C37 101.7 mm to (109.3, 110.3), turned to 90 degrees
- moved U8 98.6 mm to (106.7, 110.8), turned to 0 degrees
- moved C1 81.4 mm to (97.7, 51.8)
- moved J1 81.4 mm to (105.8, 52.7)
- moved TP3 81.4 mm to (97.7, 47.5)
- moved C103 78.7 mm to (20.3, 83.8), turned to 180 degrees
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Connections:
- J9 pad 10: /cm4/TRD3_N -> /cm4/TRD3_P
- J9 pad 3: /cm4/TRD1_P -> /cm4/TRD1_N
- J9 pad 4: /cm4/TRD1_N -> /cm4/TRD1_P
- J9 pad 9: /cm4/TRD3_P -> /cm4/TRD3_N
- R11 pad 1: /bmc/BMC_I2C_3_SCK -> /BMC ethernet/3.3v_BMC
- R11 pad 2: /BMC ethernet/3.3v_BMC -> /bmc/BMC_I2C_3_SCK
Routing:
- net /BMC ethernet/3.3v_BMC: track 552.1 -> 402.1 mm, vias 12 -> 17
- net /bmc/BMC_USB_OTG_P: track 135.3 -> 55.8 mm, vias 2 -> 0
- net /bmc/BMC_USB_OTG_N: track 133.7 -> 55.8 mm, vias 2 -> 0
- net /bmc/BMC_HOST_nRPIBOOT: track 0.00 -> 76.5 mm, vias 0 -> 4
- net /cm4/PCIE_RX_N: track 28.9 -> 104.8 mm, vias 0 -> 2
- net /cm4/PCIE_TX_N: track 31.5 -> 106.8 mm
- net /cm4/PCIE_RX_P: track 28.3 -> 103.3 mm, vias 0 -> 2
- net /cm4/PCIE_TX_P: track 30.8 -> 105.7 mm
- net /bmc/BMC_UART1_TX: track 4.83 -> 78.6 mm, vias 0 -> 4
- net /bmc/BMC_UART1_RX: track 4.97 -> 77.7 mm, vias 0 -> 2
- net /bmc/EMMC_KEY: track 119.5 -> 50.4 mm, vias 0 -> 2
- net /cm4/HDMI0_D2_P: track 110.7 -> 43.8 mm, vias 2 -> 0
- net /cm4/PCIE_CLK_N: track 25.9 -> 92.6 mm, vias 0 -> 2
- net /cm4/HDMI0_D2_N: track 110.3 -> 43.8 mm, vias 2 -> 0
- net /cm4/PCIE_CLK_P: track 25.2 -> 91.2 mm, vias 0 -> 2
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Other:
- board size 88 x 159 mm -> 104.7 x 158.5 mm
- board text removed: "1u (44mm) x 2"

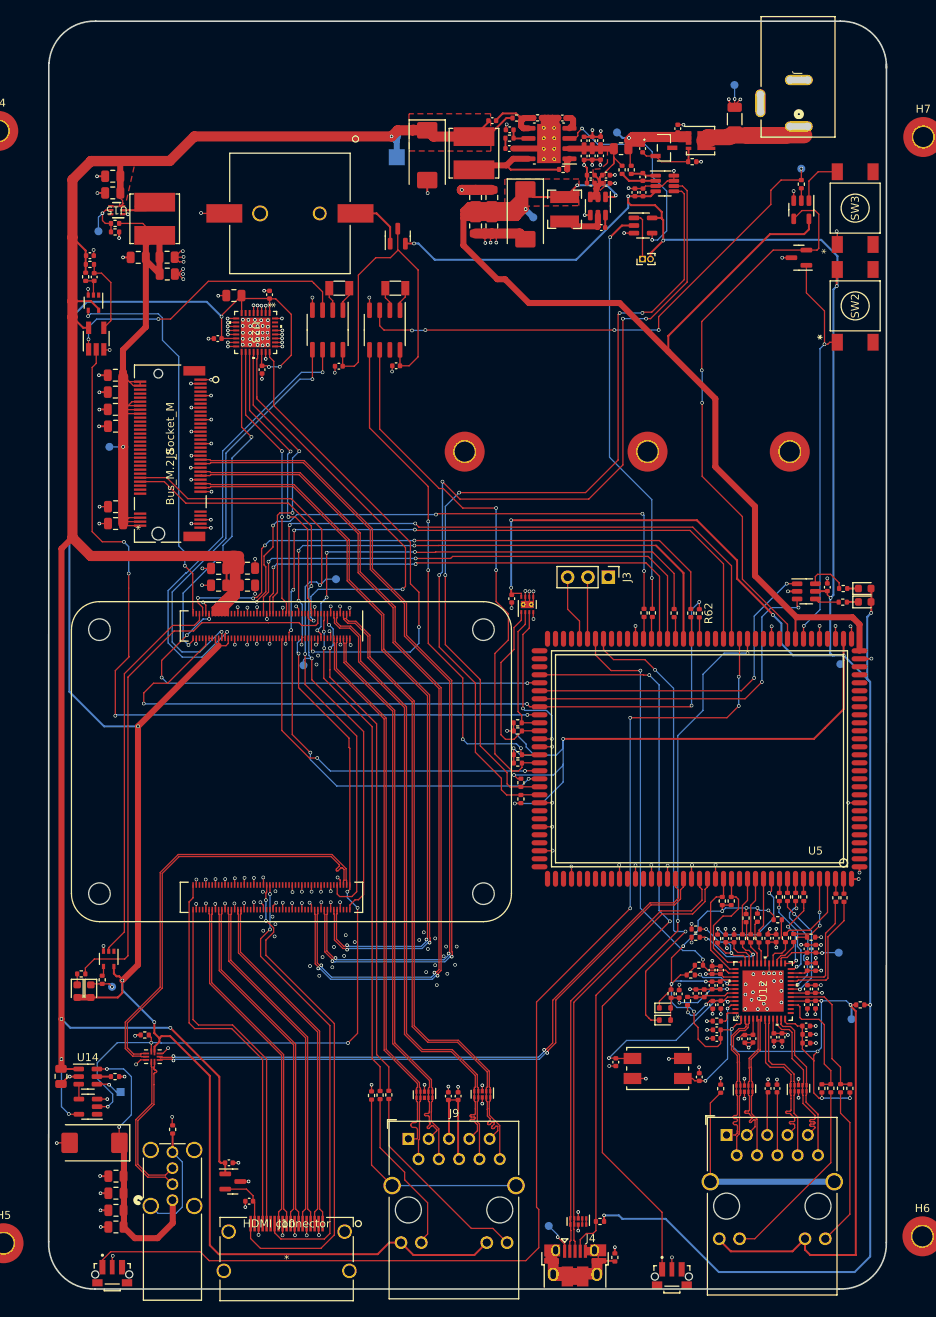
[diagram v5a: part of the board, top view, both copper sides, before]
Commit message: resolve a bunch of DRC issues
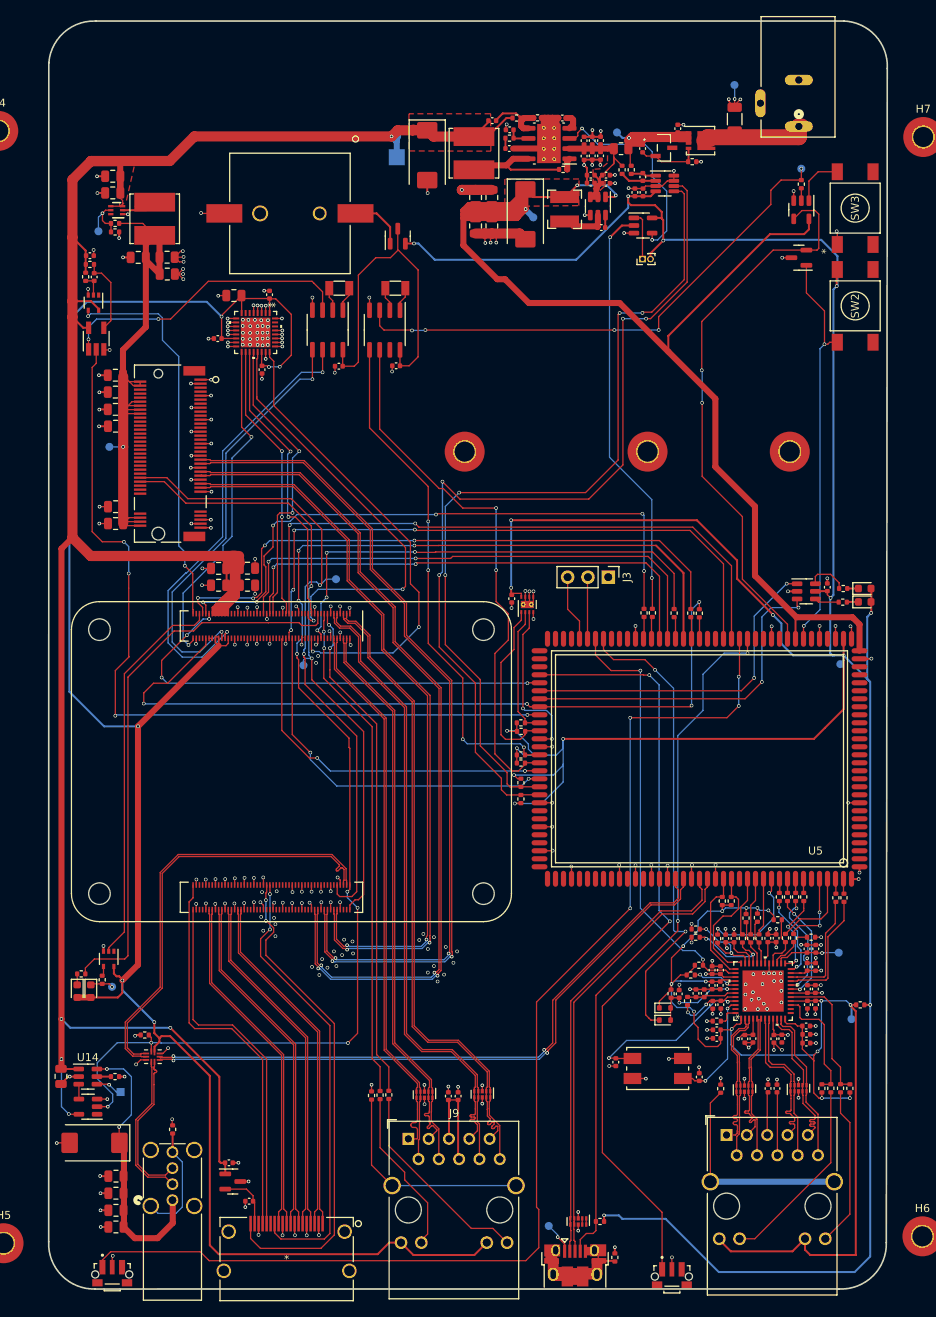
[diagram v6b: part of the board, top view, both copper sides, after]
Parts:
- moved R72 0.41 mm to (71.0, 128.3)
- moved R71 0.41 mm to (71.0, 127.3)
- moved R12 0.38 mm to (71.0, 131.3)
- moved R11 0.38 mm to (71.0, 132.3)
- moved C45 0.20 mm to (102.6, 166.8)
- moved C51 0.18 mm to (103.6, 166.8)
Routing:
- net Net-(Q1-D): track 18.4 -> 14.2 mm
- net /cm4/HOST_SPI1_MISO: track 59.6 -> 58.5 mm
- net GND: track 301.4 -> 301.6 mm, vias 312 -> 314
- added copper zone on F.Cu, net /cm4/+3.3v_HOST
- added copper zone on F.Cu, net /power/SENSE_IN-
- removed copper zone on F.Cu, net /power/SENSE_IN+
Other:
- board size 104.7 x 158.5 mm -> 104.8 x 158.5 mm
